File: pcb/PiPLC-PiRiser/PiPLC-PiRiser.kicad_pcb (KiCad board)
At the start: 2 copper layers, 51.9 x 29.6 mm, 2 parts, among them J1 Male, J2 Female

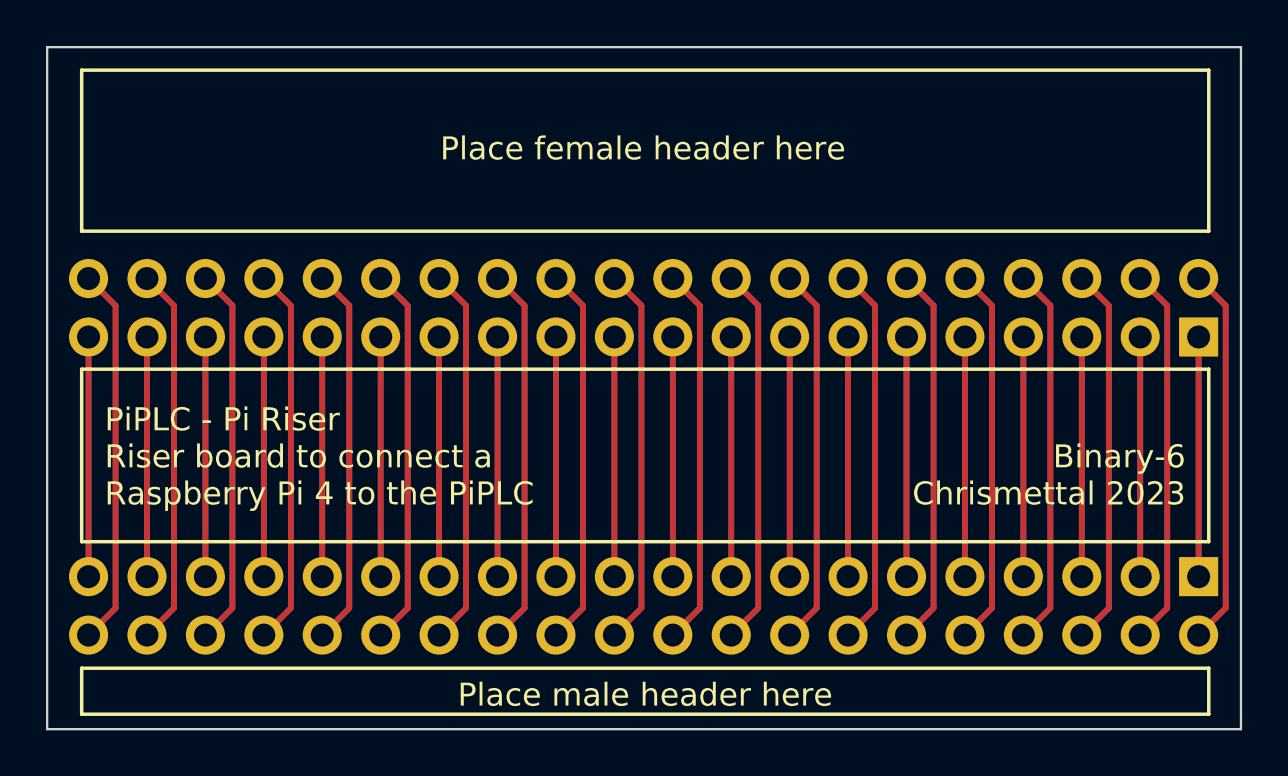
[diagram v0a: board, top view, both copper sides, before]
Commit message: [PiRiser] Reduce bottom edge by 0.25mm
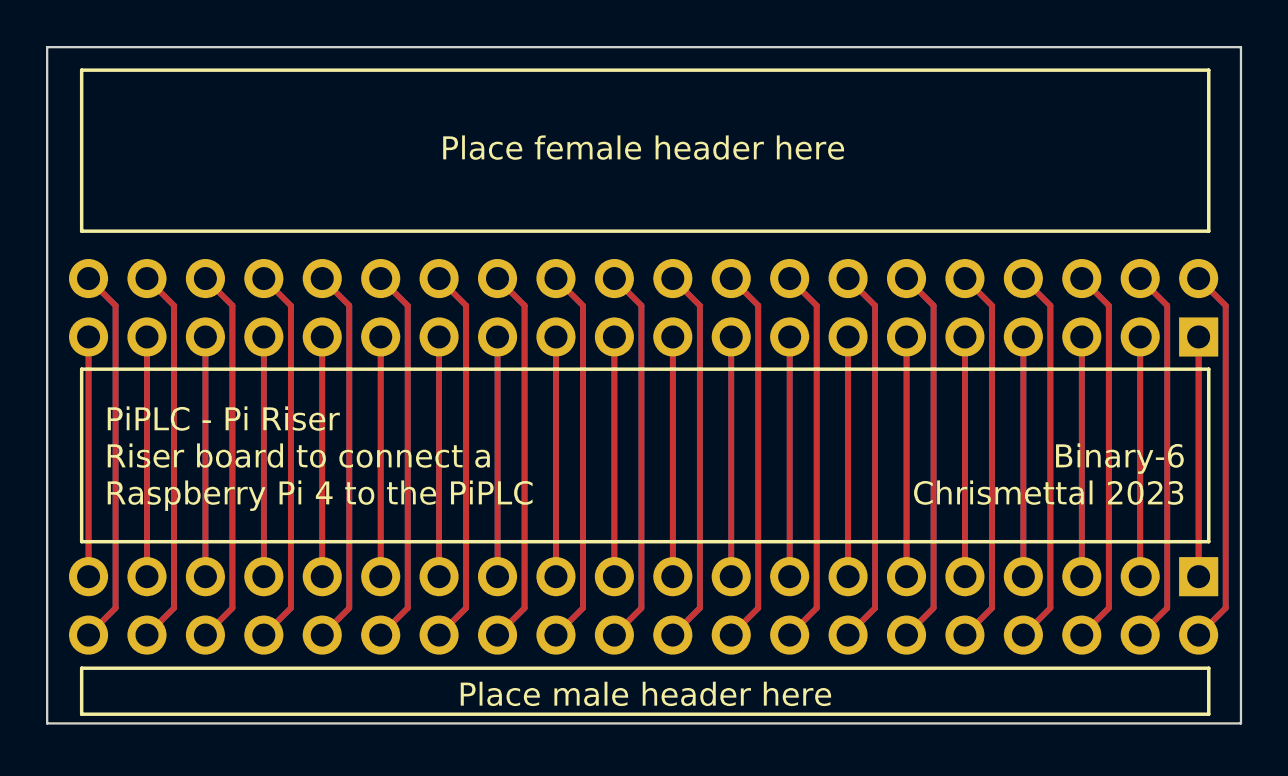
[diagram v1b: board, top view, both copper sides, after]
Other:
- board size 51.9 x 29.6 mm -> 51.9 x 29.4 mm
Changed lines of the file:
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@@
   (gr_rect (start 108.7 112.4) (end 157.7 114.4)
     (stroke (width 0.15) (type default)) (fill none) (layer "F.SilkS"))
-  (gr_rect (start 107.2 85.4) (end 159.1 115.05)
+  (gr_rect (start 107.2 85.4) (end 159.1 114.8)
     (stroke (width 0.1) (type default)) (fill none) (layer "Edge.Cuts"))
   (gr_text "This side needs to face inward of the PLC" (at 133.2 103.4) (layer "B.SilkS")
